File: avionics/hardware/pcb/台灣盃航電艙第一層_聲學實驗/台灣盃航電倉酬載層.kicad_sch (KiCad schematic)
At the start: 47 parts, among them U1 MPXV2202DPT1, U10 INA333xxDGK, U2 LM2733YMF, U3 Connector, U4 INA333xxDGK, U5 MPXV2202DPT1, U6 INA333xxDGK, U7 MPXV2202DPT1, U8 INA333xxDGK, U9 MPXV2202DPT1

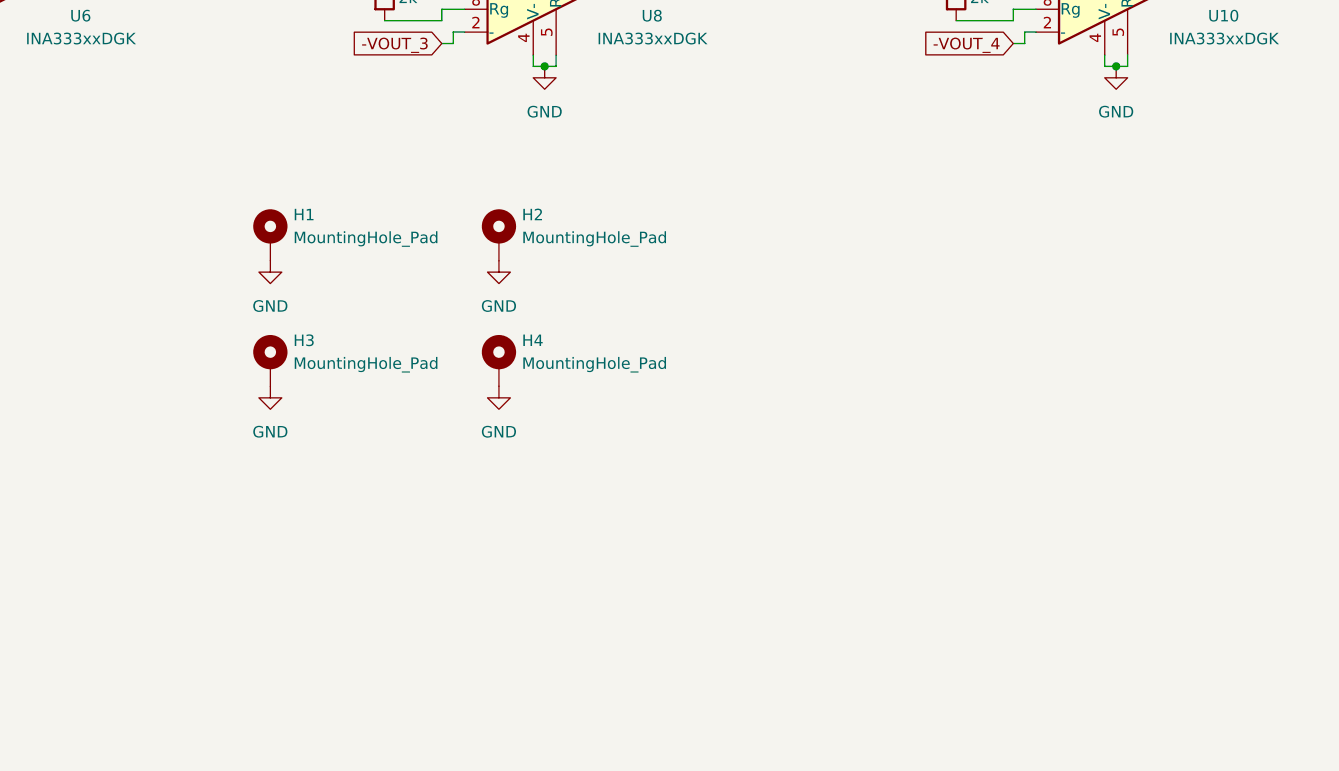
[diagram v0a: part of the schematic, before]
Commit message: 上傳新的連接器
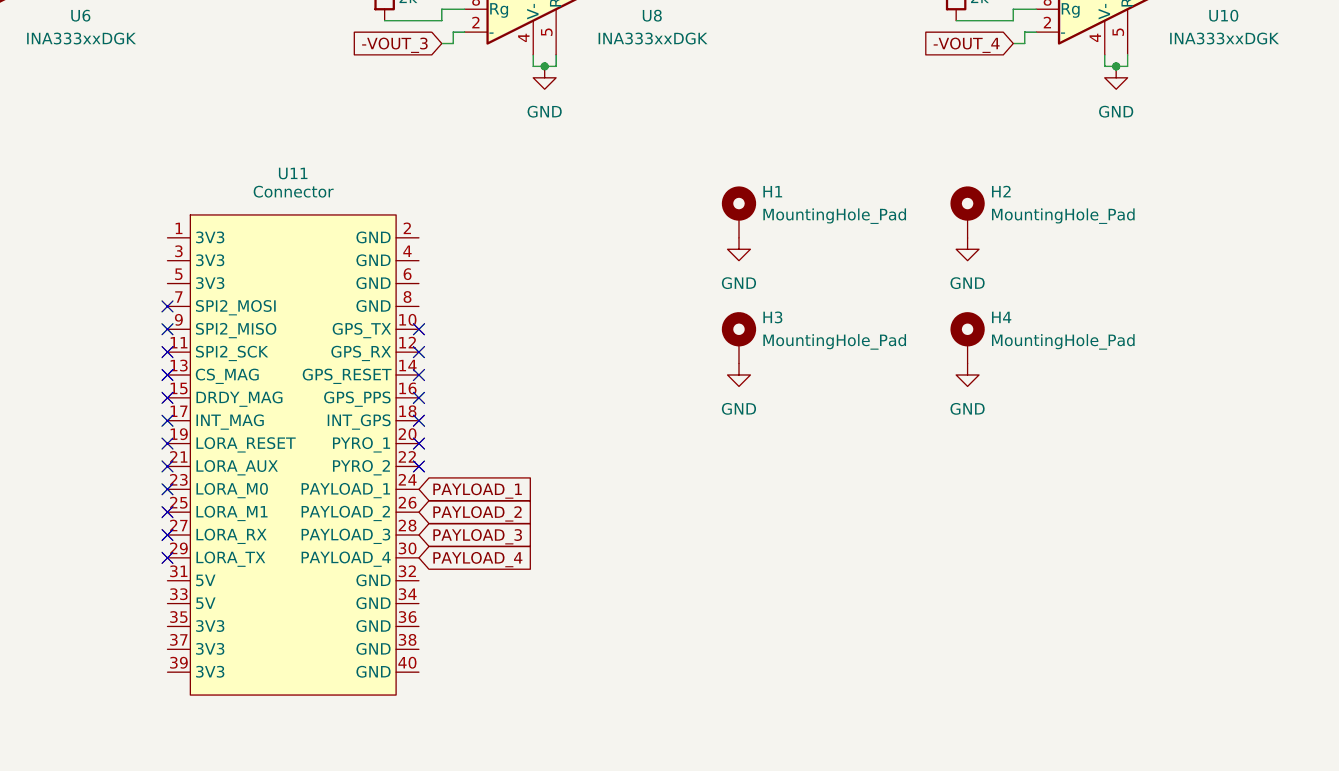
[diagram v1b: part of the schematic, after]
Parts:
- added U11: Connector, symbol MySymbol:2*20 PC104
- U3: footprint Connector_PinHeader_1.00mm:PinHeader_2x17_P1.00mm_Vertical -> Connector_PinHeader_2.54mm:PinHeader_2x20_P2.54mm_Vertical
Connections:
- net PAYLOAD_1: now also U11.24 (PAYLOAD_1)
- net PAYLOAD_2: now also U11.26 (PAYLOAD_2)
- net PAYLOAD_3: now also U11.28 (PAYLOAD_3)
- net PAYLOAD_4: now also U11.30 (PAYLOAD_4)
- no-connect marks 21 -> 40
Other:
- moved on the sheet: H1, H2, H3, H4

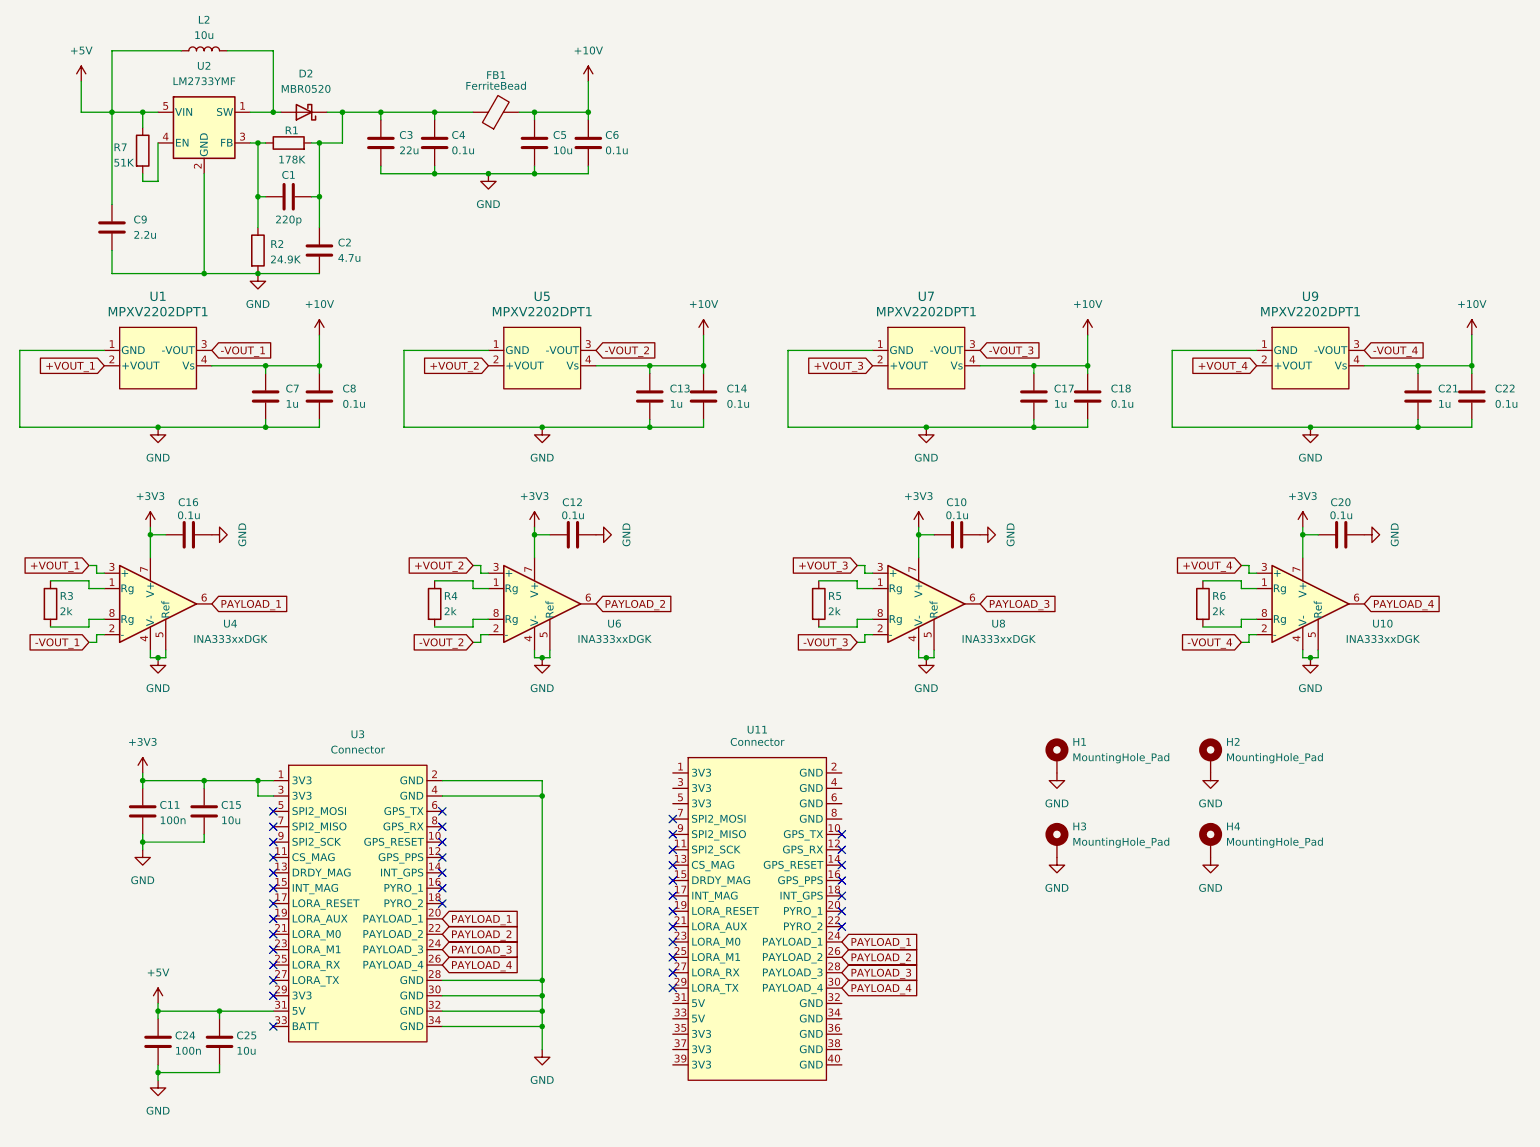
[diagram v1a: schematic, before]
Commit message: 將第一至三層連接器修改成PC104規格，第四層還未進行
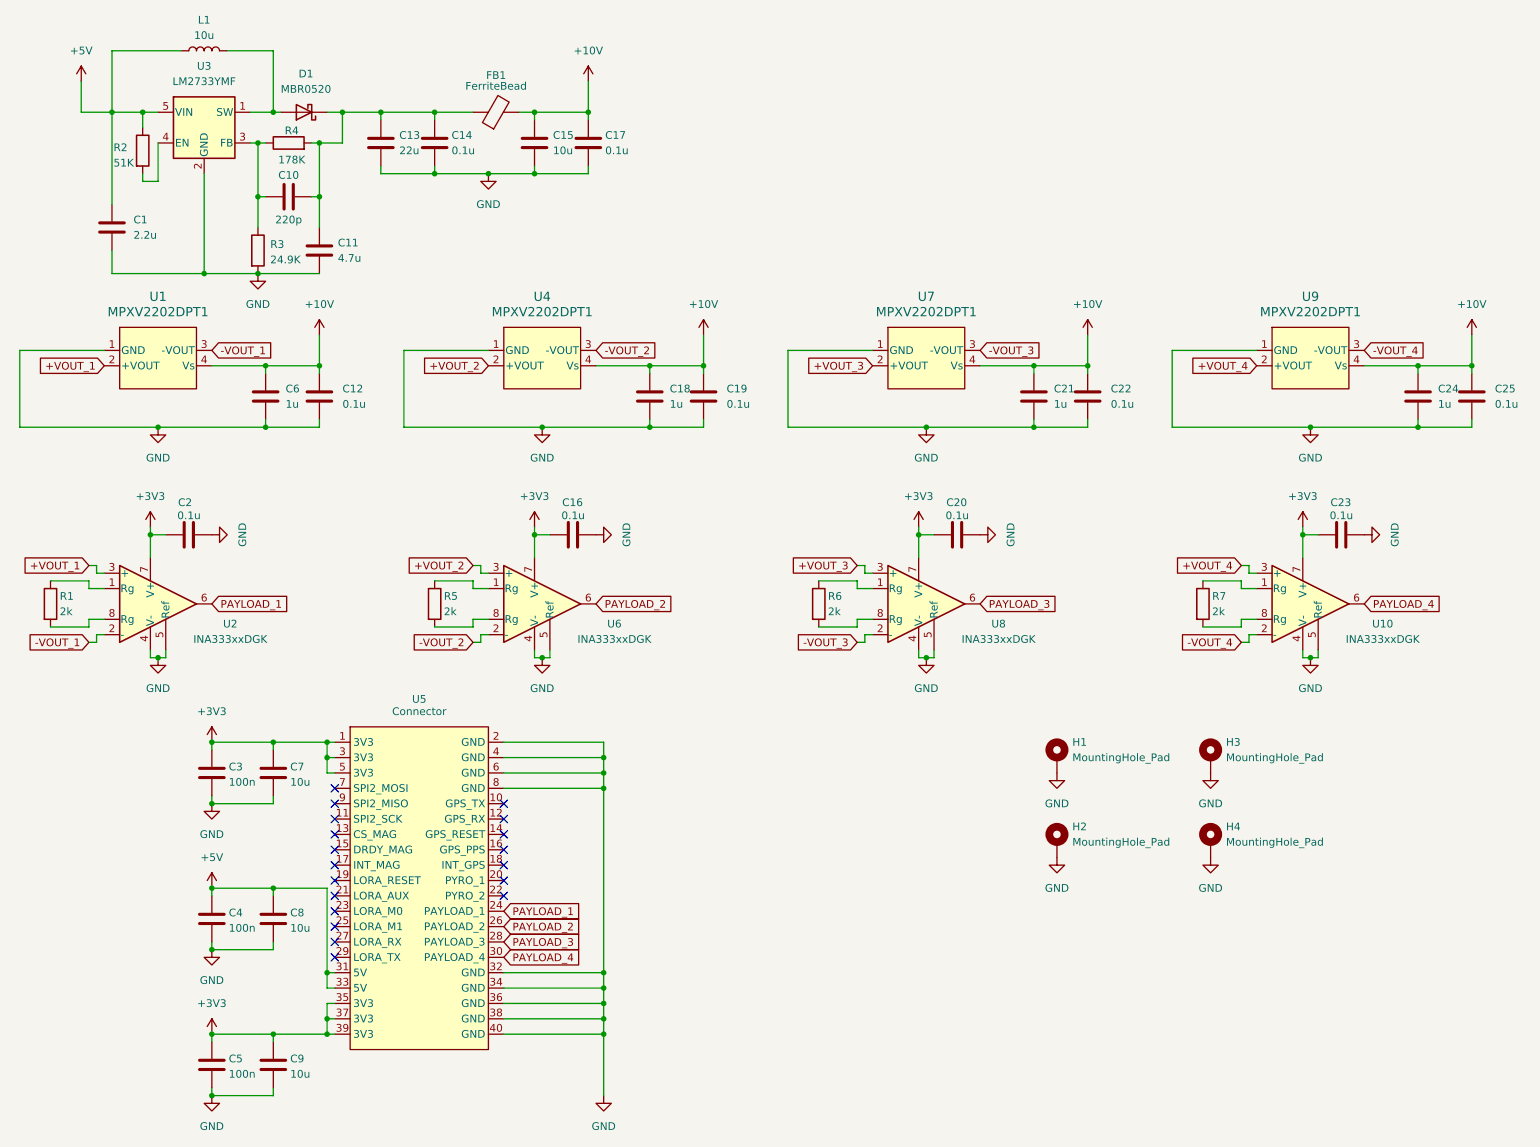
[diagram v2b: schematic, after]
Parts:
- removed C11, C24: 100n, Capacitor_SMD:C_0402_1005Metric, symbol Device:C
- removed C15, C25: 10u, Capacitor_SMD:C_0603_1608Metric, symbol Device:C
- removed U3: Connector, Connector_PinHeader_2.54mm:PinHeader_2x20_P2.54mm_Vertical, symbol MySymbol:2x17排針母座連接
- added C3, C4, C5: 100n, Capacitor_SMD:C_0402_1005Metric, symbol Device:C
- added C7, C8, C9: 10u, Capacitor_SMD:C_0603_1608Metric, symbol Device:C
- U5: renamed from U11; footprint (none) -> Connector_PinHeader_2.54mm:PinHeader_2x20_P2.54mm_Vertical
- renumbered C9 to C1, C1 to C10, C2 to C11, C8 to C12, C3 to C13, C4 to C14, C5 to C15, C12 to C16, C6 to C17, C13 to C18, C14 to C19, C16 to C2, C10 to C20, C17 to C21, C18 to C22, C20 to C23, C21 to C24, C22 to C25, C7 to C6, D2 to D1, H3 to H2, H2 to H3, L2 to L1, R3 to R1, R7 to R2, R2 to R3, R1 to R4, R4 to R5, R5 to R6, R6 to R7, U4 to U2, U2 to U3, U5 to U4
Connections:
- net +3V3: now also U5.1 (3V3), U5.3 (3V3), U5.35 (3V3), U5.37 (3V3), U5.39 (3V3), U5.5 (3V3), C3.1, C5.1, C7.1, C9.1
- net +5V: now also U5.31 (5V), U5.33 (5V), C4.1, C8.1
- net GND: now also U5.2 (GND), U5.32 (GND), U5.34 (GND), U5.36 (GND), U5.38 (GND), U5.4 (GND), U5.40 (GND), U5.6 (GND), U5.8 (GND), C3.2, C4.2, C5.2, C7.2, C8.2, C9.2
- no-connect marks 40 -> 19
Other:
- moved on the sheet: U5
